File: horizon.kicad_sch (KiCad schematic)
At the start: 36 parts, among them J2 Conn_02x03_Counter_Clockwise, J7 Conn_02x03_Counter_Clockwise, J8 Conn_02x03_Counter_Clockwise, U1 MMCU, U3 NMCU, U4 TMCU, Y1 Crystal

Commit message: fixed wiring stuff and accessories
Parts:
- removed C1, C3, C4, C5, C59, C6, C60, C8: 100nF, symbol Device:C
- removed C2, C7: 10uF, symbol Device:C
- removed L5, L6: SLF7055T-6R8N2R8-3PF, Inductor_SMD:L_7.3x7.3_H4.5, symbol SLF7055T-6R8N2R8-3PF[1]:SLF7055T-6R8N2R8-3PF
- added C63: 1uF, symbol Device:C
- added C64, C65, C66: 0.1uF, symbol Device:C
- added C67: 4.7uF, symbol Device:C
- added C68, C69, C70, C71, C72, C73, C74, C75, C76, C77, C78: 100nF, symbol Device:C
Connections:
- net +3.3V: now also U3.8 (VDDANA), U4.8 (VDDANA), C63.1, C64.1, C65.1, C66.1, C68.2, C69.2, C70.2, C71.2, C73.2, C74.2, C75.2, C76.2, C77.2; no longer C10.2, C11.2, C12.2, C13.2, C17.2, C61.1, C62.1, C9.2, J2.3 (Pin_3), J7.3 (Pin_3), J8.3 (Pin_3), U1.10 (A10/ADC0_DM0), U1.15 (VREF-L), U1.16 (VSSA), U1.17 (VREF_OUT), U1.31 (VSS), U1.4 (VSS), U1.47 (VSS), U1.7 (VOUT3V3), U3.22 (GND), U3.33 (GND), U3.47 (GND), U3.54 (GND), U3.7 (GNDANA), U4.22 (GND), U4.33 (GND), U4.47 (GND), U4.54 (GND), U4.7 (GNDANA)
- net at U3.55 (VDDCORE): now also C72.2
- net 1R: now reaches U1.28 (D3/CAN-TX/PWM)
- net 1G: now reaches U1.46 (D9/RX2/PWM)
- net 1B: now reaches U1.49 (D10/TX2/PWM)
- net 2R: now reaches U4.61 (PB00)
- net 2G: now reaches U4.62 (PB01)
- net 2B: now reaches U4.64 (PB03)
- net 3R: now reaches U3.61 (PB00)
- net 3G: now reaches U3.62 (PB01)
- net 3B: now reaches U3.63 (PB02)
- new net: C67.1, U1.7 (VOUT3V3)
- new net: C78.2, U4.7 (GNDANA)
- new net GND: C10.2, C11.2, C12.2, C13.2, C17.2, C61.1, C62.1, C63.2, C64.2, C65.2, C66.2, C67.2, C68.1, C69.1, C70.1, C71.1, C72.1, C73.1, C74.1, C75.1, C76.1, C77.1, C78.1, C9.2, J2.3 (Pin_3), J7.3 (Pin_3), J8.3 (Pin_3), U1.15 (VREF-L), U1.16 (VSSA), U1.31 (VSS), U1.4 (VSS), U1.47 (VSS), U3.22 (GND), U3.33 (GND), U3.47 (GND), U3.54 (GND), U3.7 (GNDANA), U4.22 (GND), U4.33 (GND), U4.47 (GND), U4.54 (GND)
- no-connect marks 98 -> 90
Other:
- note removed: "Set low to talk to BARO"
- moved on the sheet: C11, C12, C13, C9, R28

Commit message: footprints
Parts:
- C10, C11, C9: footprint (none) -> Capacitor_SMD:C_0603_1608Metric
- C12, C13, C17, C61, C62, C63, C64, C65, C66, C67, C68, C69, C70, C71, C72, C73, C74, C75, C76, C77, C78: footprint (none) -> Capacitor_SMD:C_0201_0603Metric
- R26, R28, R29, R3, R30, R4, R5, R6, R7: footprint (none) -> Resistor_SMD:R_0603_1608Metric
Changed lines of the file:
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@@
 			)
 		)
-		(property "Footprint" ""
+		(property "Footprint" "Resistor_SMD:R_0603_1608Metric"
 			(at 31.242 175.26 90)
 			(effects
@@
 			)
 		)
-		(property "Footprint" ""
+		(property "Footprint" "Capacitor_SMD:C_0201_0603Metric"
 			(at 148.59 54.9148 0)
 			(effects
@@
 			)
 		)
-		(property "Footprint" ""
+		(property "Footprint" "Resistor_SMD:R_0603_1608Metric"
 			(at 176.022 76.2 90)
 			(effects
@@
 			)
 		)
-		(property "Footprint" ""
+		(property "Footprint" "Capacitor_SMD:C_0201_0603Metric"
 			(at 148.59 53.0352 0)
 			(effects
@@
 			)
 		)
-		(property "Footprint" ""
+		(property "Footprint" "Resistor_SMD:R_0603_1608Metric"
 			(at 248.412 170.18 90)
 			(effects
@@
 			)
 		)
-		(property "Footprint" ""
+		(property "Footprint" "Capacitor_SMD:C_0201_0603Metric"
 			(at 281.6352 77.47 0)
 			(effects
@@
 			)
 		)
-		(property "Footprint" ""
+		(property "Footprint" "Capacitor_SMD:C_0201_0603Metric"
 			(at 148.59 49.8348 0)
 			(effects
@@
 			)
 		)
-		(property "Footprint" ""
+		(property "Footprint" "Capacitor_SMD:C_0201_0603Metric"
 			(at 148.59 58.1152 0)
 			(effects
@@
 			)
 		)
-		(property "Footprint" ""
+		(property "Footprint" "Resistor_SMD:R_0603_1608Metric"
 			(at 107.442 109.22 90)
 			(effects
@@
 			)
 		)
-		(property "Footprint" ""
+		(property "Footprint" "Capacitor_SMD:C_0201_0603Metric"
 			(at 43.18 54.9148 0)
 			(effects
@@
 			)
 		)
-		(property "Footprint" ""
+		(property "Footprint" "Resistor_SMD:R_0603_1608Metric"
 			(at 201.422 96.52 90)
 			(effects
@@
 			)
 		)
-		(property "Footprint" ""
+		(property "Footprint" "Capacitor_SMD:C_0201_0603Metric"
 			(at 280.9748 44.45 0)
 			(effects
@@
 			)
 		)
-		(property "Footprint" ""
+		(property "Footprint" "Capacitor_SMD:C_0201_0603Metric"
 			(at 341.9348 39.37 0)
 			(effects
@@
 			)
 		)
-		(property "Footprint" ""
+		(property "Footprint" "Capacitor_SMD:C_0603_1608Metric"
 			(at 294.64 109.5248 0)
 			(effects
@@
 			)
 		)
-		(property "Footprint" ""
+		(property "Footprint" "Resistor_SMD:R_0603_1608Metric"
 			(at 136.652 181.61 90)
 			(effects
@@
 			)
 		)
-		(property "Footprint" ""
+		(property "Footprint" "Capacitor_SMD:C_0201_0603Metric"
 			(at 53.34 46.0248 0)
 			(effects
@@
 			)
 		)
-		(property "Footprint" ""
+		(property "Footprint" "Capacitor_SMD:C_0201_0603Metric"
 			(at 288.29 103.1748 0)
 			(effects
@@
 			)
 		)
-		(property "Footprint" ""
+		(property "Footprint" "Capacitor_SMD:C_0201_0603Metric"
 			(at 288.29 53.6448 0)
 			(effects
@@
 			)
 		)
-		(property "Footprint" ""
+		(property "Footprint" "Capacitor_SMD:C_0201_0603Metric"
 			(at 53.34 54.3052 0)
 			(effects
@@
 			)
 		)
-		(property "Footprint" ""
+		(property "Footprint" "Capacitor_SMD:C_0201_0603Metric"
 			(at 345.1352 57.15 0)
 			(effects
@@
 			)
 		)
-		(property "Footprint" ""
+		(property "Footprint" "Capacitor_SMD:C_0201_0603Metric"
 			(at 53.34 49.2252 0)
 			(effects
@@
 			)
 		)
-		(property "Footprint" ""
+		(property "Footprint" "Capacitor_SMD:C_0201_0603Metric"
 			(at 53.34 51.1048 0)
 			(effects
@@
 			)
 		)
-		(property "Footprint" ""
+		(property "Footprint" "Capacitor_SMD:C_0201_0603Metric"
 			(at 148.59 157.1752 0)
 			(effects
@@
 			)
 		)
-		(property "Footprint" ""
+		(property "Footprint" "Capacitor_SMD:C_0201_0603Metric"
 			(at 294.64 117.1448 0)
 			(effects
@@
 			)
 		)
-		(property "Footprint" ""
+		(property "Footprint" "Capacitor_SMD:C_0603_1608Metric"
 			(at 341.3252 62.23 0)
 			(effects
@@
 			)
 		)
-		(property "Footprint" ""
+		(property "Footprint" "Resistor_SMD:R_0603_1608Metric"
 			(at 216.408 114.3 90)
 			(effects
@@
 			)
 		)
-		(property "Footprint" ""
+		(property "Footprint" "Capacitor_SMD:C_0201_0603Metric"
 			(at 138.43 58.7248 0)
 			(effects
@@
 			)
 		)
-		(property "Footprint" ""
+		(property "Footprint" "Capacitor_SMD:C_0201_0603Metric"
 			(at 53.34 44.1452 0)
 			(effects
@@
 			)
 		)
-		(property "Footprint" ""
+		(property "Footprint" "Resistor_SMD:R_0603_1608Metric"
 			(at 198.882 124.46 90)
 			(effects
@@
 			)
 		)
-		(property "Footprint" ""
+		(property "Footprint" "Capacitor_SMD:C_0201_0603Metric"
 			(at 281.6352 67.31 0)
 			(effects
@@
 			)
 		)
-		(property "Footprint" ""
+		(property "Footprint" "Resistor_SMD:R_0603_1608Metric"
 			(at 192.532 127 90)
 			(effects
@@
 			)
 		)
-		(property "Footprint" ""
+		(property "Footprint" "Capacitor_SMD:C_0201_0603Metric"
 			(at 148.59 47.9552 0)
 			(effects
@@
 			)
 		)
-		(property "Footprint" ""
+		(property "Footprint" "Capacitor_SMD:C_0603_1608Metric"
 			(at 341.3252 72.39 0)
 			(effects

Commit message: clean up
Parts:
- removed C11, C9: C, Capacitor_SMD:C_0603_1608Metric, symbol Device:C
- removed C12, C13: C, Capacitor_SMD:C_0201_0603Metric, symbol Device:C

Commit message: i fogro
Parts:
- C72: value 100nF -> 1uF
- J2, J7, J8: footprint (none) -> Connector_PinSocket_2.54mm:PinSocket_2x03_P2.54mm_Vertical
- Y1: footprint (none) -> Crystal:Crystal_SMD_0603-2Pin_6.0x3.5mm
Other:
- moved on the sheet: C10, C17, C61, C62, C63, C64, C65, C66, C67, C68, C69, C70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

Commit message: started pcb
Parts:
- C17, C61, C62, C63, C64, C65, C66, C67, C68, C69, C70, C71, C72, C73, C74, C75, C76, C77, C78: footprint Capacitor_SMD:C_0201_0603Metric -> Capacitor_SMD:C_0603_1608Metric
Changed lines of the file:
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@@
 			)
 		)
-		(property "Footprint" "Capacitor_SMD:C_0201_0603Metric"
+		(property "Footprint" "Capacitor_SMD:C_0603_1608Metric"
 			(at 147.32 32.0548 0)
 			(effects
@@
 			)
 		)
-		(property "Footprint" "Capacitor_SMD:C_0201_0603Metric"
+		(property "Footprint" "Capacitor_SMD:C_0603_1608Metric"
 			(at 147.32 30.1752 0)
 			(effects
@@
 			)
 		)
-		(property "Footprint" "Capacitor_SMD:C_0201_0603Metric"
+		(property "Footprint" "Capacitor_SMD:C_0603_1608Metric"
 			(at 280.3652 54.61 0)
 			(effects
@@
 			)
 		)
-		(property "Footprint" "Capacitor_SMD:C_0201_0603Metric"
+		(property "Footprint" "Capacitor_SMD:C_0603_1608Metric"
 			(at 147.32 26.9748 0)
 			(effects
@@
 			)
 		)
-		(property "Footprint" "Capacitor_SMD:C_0201_0603Metric"
+		(property "Footprint" "Capacitor_SMD:C_0603_1608Metric"
 			(at 147.32 35.2552 0)
 			(effects
@@
 			)
 		)
-		(property "Footprint" "Capacitor_SMD:C_0201_0603Metric"
+		(property "Footprint" "Capacitor_SMD:C_0603_1608Metric"
 			(at 41.91 32.0548 0)
 			(effects
@@
 			)
 		)
-		(property "Footprint" "Capacitor_SMD:C_0201_0603Metric"
+		(property "Footprint" "Capacitor_SMD:C_0603_1608Metric"
 			(at 279.7048 21.59 0)
 			(effects
@@
 			)
 		)
-		(property "Footprint" "Capacitor_SMD:C_0201_0603Metric"
+		(property "Footprint" "Capacitor_SMD:C_0603_1608Metric"
 			(at 52.07 23.1648 0)
 			(effects
@@
 			)
 		)
-		(property "Footprint" "Capacitor_SMD:C_0201_0603Metric"
+		(property "Footprint" "Capacitor_SMD:C_0603_1608Metric"
 			(at 287.02 80.3148 0)
 			(effects
@@
 			)
 		)
-		(property "Footprint" "Capacitor_SMD:C_0201_0603Metric"
+		(property "Footprint" "Capacitor_SMD:C_0603_1608Metric"
 			(at 287.02 30.7848 0)
 			(effects
@@
 			)
 		)
-		(property "Footprint" "Capacitor_SMD:C_0201_0603Metric"
+		(property "Footprint" "Capacitor_SMD:C_0603_1608Metric"
 			(at 52.07 31.4452 0)
 			(effects
@@
 			)
 		)
-		(property "Footprint" "Capacitor_SMD:C_0201_0603Metric"
+		(property "Footprint" "Capacitor_SMD:C_0603_1608Metric"
 			(at 52.07 26.3652 0)
 			(effects
@@
 			)
 		)
-		(property "Footprint" "Capacitor_SMD:C_0201_0603Metric"
+		(property "Footprint" "Capacitor_SMD:C_0603_1608Metric"
 			(at 52.07 28.2448 0)
 			(effects
@@
 			)
 		)
-		(property "Footprint" "Capacitor_SMD:C_0201_0603Metric"
+		(property "Footprint" "Capacitor_SMD:C_0603_1608Metric"
 			(at 147.32 134.3152 0)
 			(effects
@@
 			)
 		)
-		(property "Footprint" "Capacitor_SMD:C_0201_0603Metric"
+		(property "Footprint" "Capacitor_SMD:C_0603_1608Metric"
 			(at 293.37 94.2848 0)
 			(effects
@@
 			)
 		)
-		(property "Footprint" "Capacitor_SMD:C_0201_0603Metric"
+		(property "Footprint" "Capacitor_SMD:C_0603_1608Metric"
 			(at 137.16 35.8648 0)
 			(effects
@@
 			)
 		)
-		(property "Footprint" "Capacitor_SMD:C_0201_0603Metric"
+		(property "Footprint" "Capacitor_SMD:C_0603_1608Metric"
 			(at 52.07 21.2852 0)
 			(effects
@@
 			)
 		)
-		(property "Footprint" "Capacitor_SMD:C_0201_0603Metric"
+		(property "Footprint" "Capacitor_SMD:C_0603_1608Metric"
 			(at 280.3652 44.45 0)
 			(effects
@@
 			)
 		)
-		(property "Footprint" "Capacitor_SMD:C_0201_0603Metric"
+		(property "Footprint" "Capacitor_SMD:C_0603_1608Metric"
 			(at 147.32 25.0952 0)
 			(effects

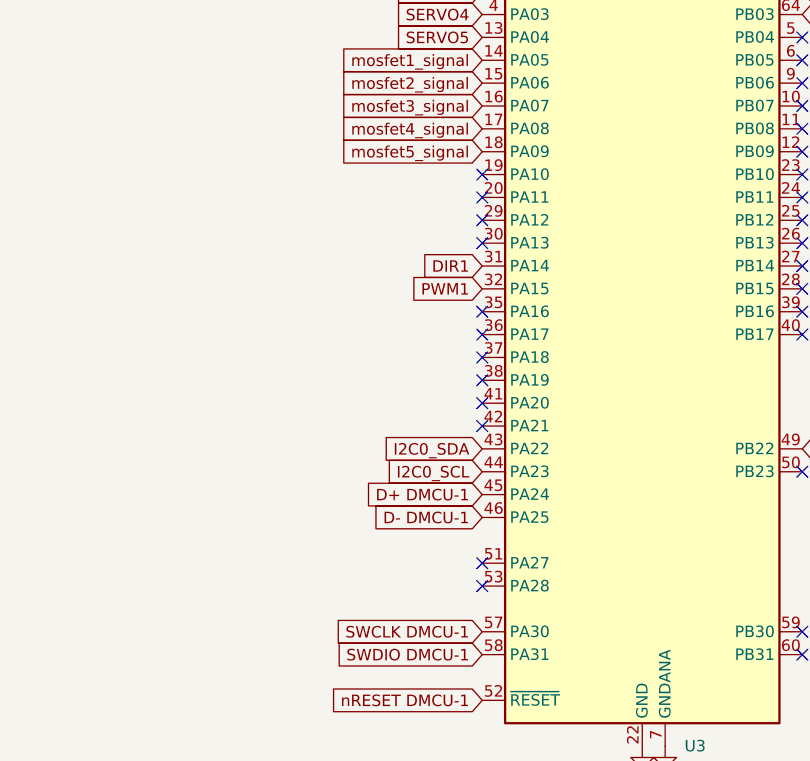
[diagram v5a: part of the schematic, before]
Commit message: Hopefully added BL, and all the remaining footprints
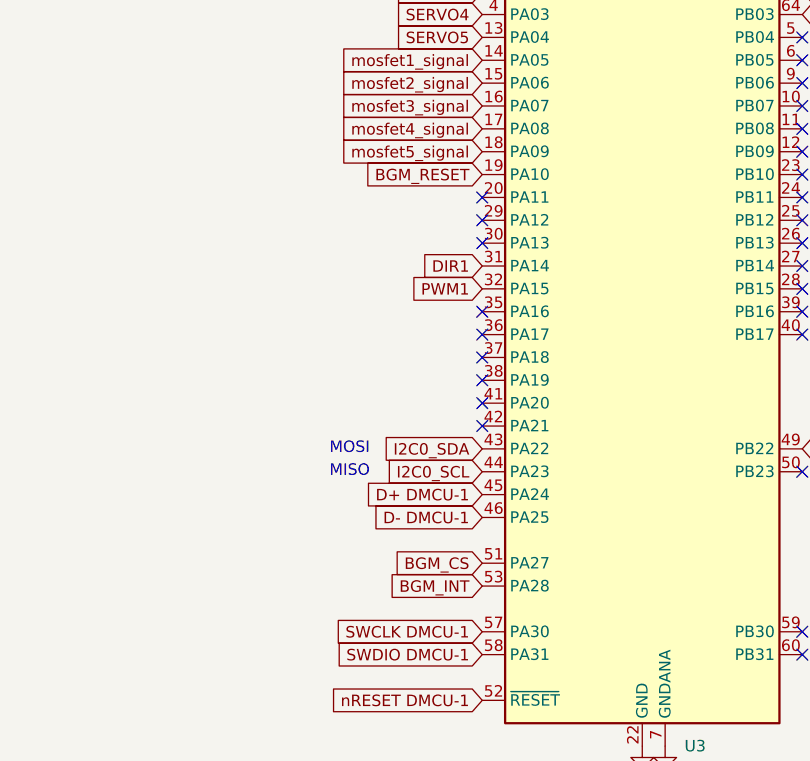
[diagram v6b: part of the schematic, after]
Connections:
- net BGM_RESET: now reaches U3.19 (PA10)
- net BGM_CS: now reaches U3.51 (PA27)
- net BGM_INT: now reaches U3.53 (PA28)
- no-connect marks 90 -> 87
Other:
- note added: "MISO"
- note added: "MOSI"
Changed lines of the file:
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@@
+		)
+	)
+	(text "MOSI"
+		(exclude_from_sim no)
+		(at 17.018 96.52 0)
+		(effects
+			(font
+				(size 1.27 1.27)
+			)
 		)
 	)
@@
 		)
 	)
+	(text "MISO"
+		(exclude_from_sim no)
+		(at 17.018 99.06 0)
+		(effects
+			(font
+				(size 1.27 1.27)
+			)
+		)
+	)
 	(junction
 		(at 31.75 148.59)
@@
 	)
 	(no_connect
-		(at 31.75 109.22)
-	)
-	(no_connect
 		(at 220.98 128.27)
 	)
@@
 	)
 	(no_connect
-		(at 31.75 66.04)
-	)
-	(no_connect
 		(at 162.56 100.33)
 	)
@@
 	)
 	(no_connect
-		(at 31.75 111.76)
-	)
-	(no_connect
 		(at 127 44.45)
 	)
@@
 		)
 	)
+	(global_label "BGM_INT"
+		(shape input)
+		(at 31.75 111.76 180)
+		(fields_autoplaced yes)
+		(effects
+			(font
+				(size 1.27 1.27)
+			)
+			(justify right)
+		)
+		(property "Intersheetrefs" "${INTERSHEET_REFS}"
+			(at 20.9029 111.76 0)
+			(effects
+				(font
+					(size 1.27 1.27)
+				)
+				(justify right)
+				(hide yes)
+			)
+		)
+	)
 	(global_label "mosfet4_signal"
 		(shape input)
@@
 		)
 	)
+	(global_label "BGM_RESET"
+		(shape input)
+		(at 31.75 66.04 180)
+		(fields_autoplaced yes)
+		(effects
+			(font
+				(size 1.27 1.27)
+			)
+			(justify right)
+		)
+		(property "Intersheetrefs" "${INTERSHEET_REFS}"
+			(at 18.0607 66.04 0)
+			(effects
+				(font
+					(size 1.27 1.27)
+				)
+				(justify right)
+				(hide yes)
+			)
+		)
+	)
 	(global_label "PTA12"
 		(shape input)
@@
 			(effects
 				(font
+					(size 1.27 1.27)
+				)
+				(justify right)
+				(hide yes)
+			)
+		)
+	)
+	(global_label "BGM_CS"
+		(shape input)
+		(at 31.75 109.22 180)
+		(fields_autoplaced yes)
+		(effects
+			(font
+				(size 1.27 1.27)
+			)
+			(justify right)
+		)
+		(property "Intersheetrefs" "${INTERSHEET_REFS}"
+			(at 21.3263 109.22 0)
+			(effects
+				(font

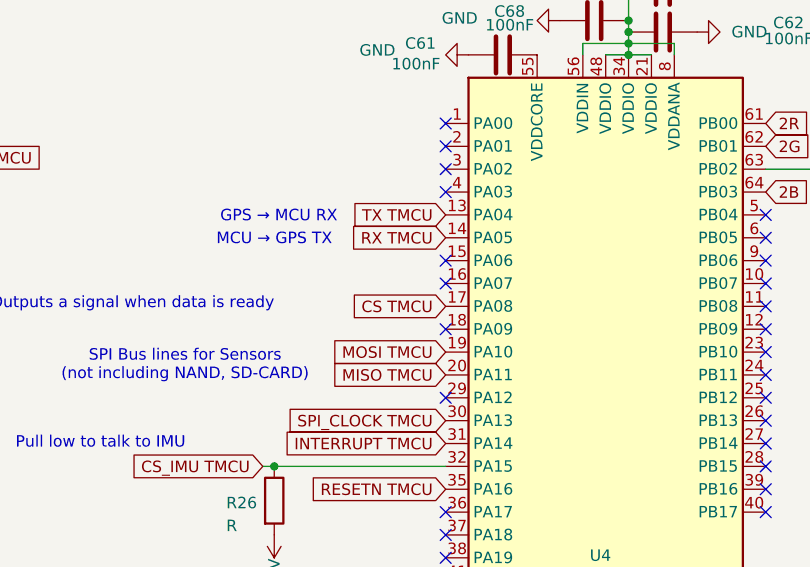
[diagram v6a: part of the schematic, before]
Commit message: CS, and SCK for RF
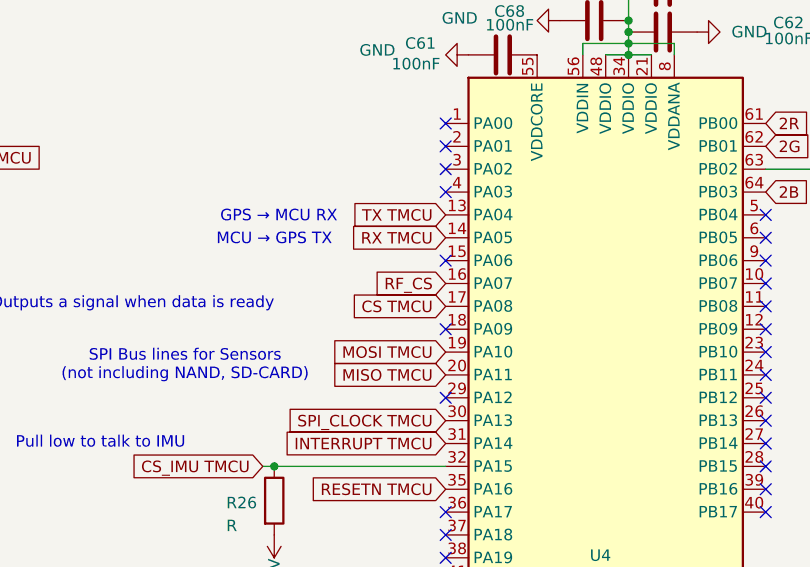
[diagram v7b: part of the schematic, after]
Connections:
- net RF_CS: now reaches U4.16 (PA07)
- no-connect marks 87 -> 86
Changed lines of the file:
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@@
-	)
-	(no_connect
-		(at 127 62.23)
 	)
 	(no_connect
@@
 			(effects
 				(font
+					(size 1.27 1.27)
+				)
+				(justify right)
+				(hide yes)
+			)
+		)
+	)
+	(global_label "RF_CS"
+		(shape input)
+		(at 127 62.23 180)
+		(fields_autoplaced yes)
+		(effects
+			(font
+				(size 1.27 1.27)
+			)
+			(justify right)
+		)
+		(property "Intersheetrefs" "${INTERSHEET_REFS}"
+			(at 118.2091 62.23 0)
+			(effects
+				(font

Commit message: do some rf routing (and hopefully not break everything)
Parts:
- U1: footprint MK20DX256VLH7:QFP50P1200X1200X160-64N -> MMCU:QFP50P1200X1200X160-64N
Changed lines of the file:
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@@
 			)
 		)
-		(property "Footprint" "MK20DX256VLH7:QFP50P1200X1200X160-64N"
+		(property "Footprint" "MMCU:QFP50P1200X1200X160-64N"
 			(at 248.92 82.55 0)
 			(effects
